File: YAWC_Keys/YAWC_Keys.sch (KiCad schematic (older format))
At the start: 19 parts, among them P1 K1, P10 K10, P11 K11, P2 K2, P3 K3, P4 K4, P5 K5, P6 K6, P7 K7, P8 K8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

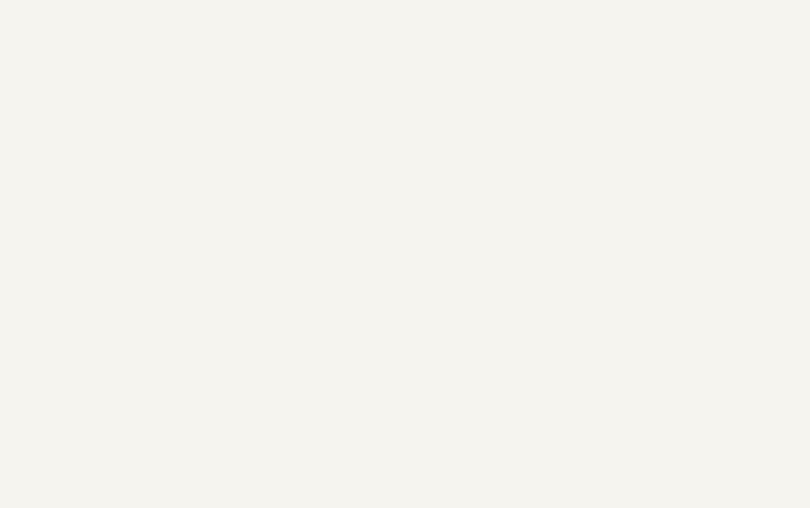
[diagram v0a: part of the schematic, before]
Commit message: Add route plugs for breath amp through to main board via keys. Add straight 1x6 header
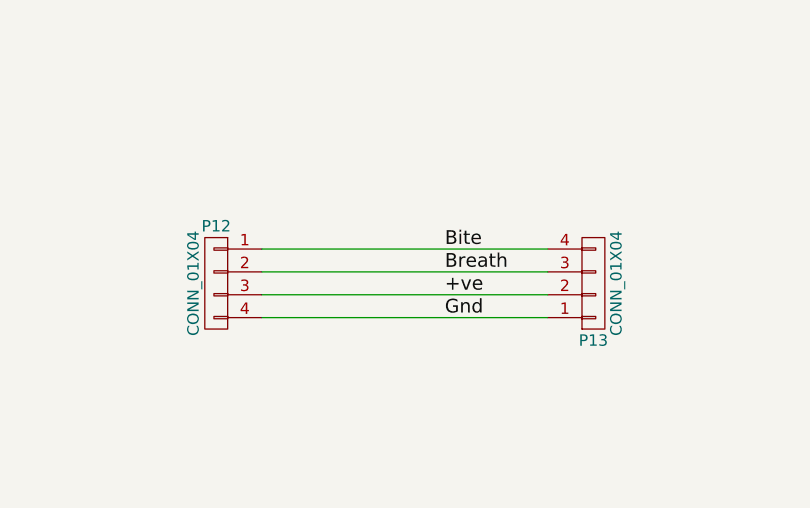
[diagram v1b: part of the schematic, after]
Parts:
- added P12: CONN_01X04, My_Pin_Headers:Pin_Header_Angled_1x04, symbol CONN_01X04
- added P13: CONN_01X04, My_Pin_Headers:Pin_Header_Straight_1x04, symbol CONN_01X04
- PLh1: footprint PIN_Hdr:Pin_Header_1x05 -> My_Pin_Headers:Pin_Header_Straight_1x05
- PRh1: footprint PIN_Hdr:Pin_Header_1x06 -> My_Pin_Headers:Pin_Header_Straight_1x06
- PTh1: footprint PIN_Hdr:Pin_Header_Angled_1x05 -> My_Pin_Headers:Pin_Header_Angled_1x05
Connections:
- new net +ve: P12.3 (P3), P13.2 (P2)
- new net Bite: P12.1 (P1), P13.4 (P4)
- new net Breath: P12.2 (P2), P13.3 (P3)
- new net Gnd: P12.4 (P4), P13.1 (P1)
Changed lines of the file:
@@
 F 0 "PLh1" H 5750 2100 50  0000 C CNN
 F 1 "CONN_01X05" V 5850 1800 50  0000 C CNN
-F 2 "PIN_Hdr:Pin_Header_1x05" H 5750 1800 50  0001 C CNN
+F 2 "My_Pin_Headers:Pin_Header_Straight_1x05" H 5750 1800 50  0001 C CNN
 F 3 "" H 5750 1800 50  0000 C CNN
 	1    5750 1800
@@
 F 0 "PTh1" H 5900 4300 50  0000 C CNN
 F 1 "CONN_01X05" V 6000 4000 50  0000 C CNN
-F 2 "PIN_Hdr:Pin_Header_Angled_1x05" H 5900 4000 50  0001 C CNN
+F 2 "My_Pin_Headers:Pin_Header_Angled_1x05" H 5900 4000 50  0001 C CNN
 F 3 "" H 5900 4000 50  0000 C CNN
 	1    5900 4000
@@
 F 0 "PRh1" H 9600 2250 50  0000 C CNN
 F 1 "CONN_01X06" V 9700 1900 50  0000 C CNN
-F 2 "PIN_Hdr:Pin_Header_1x06" H 9600 1900 50  0001 C CNN
+F 2 "My_Pin_Headers:Pin_Header_Straight_1x06" H 9600 1900 50  0001 C CNN
 F 3 "" H 9600 1900 50  0000 C CNN
 	1    9600 1900
@@
 Text Notes 6850 1400 0    197  ~ 0
 Right Hand
+$Comp
+L CONN_01X04 P12
+U 1 1 56EFDACE
+P 7050 3950
+F 0 "P12" H 7050 4200 50  0000 C CNN
+F 1 "CONN_01X04" V 7150 3950 50  0000 C CNN
+F 2 "My_Pin_Headers:Pin_Header_Angled_1x04" H 7050 3950 50  0001 C CNN
+F 3 "" H 7050 3950 50  0000 C CNN
+	1    7050 3950
+	-1   0    0    -1
+$EndComp
+$Comp
+L CONN_01X04 P13
+U 1 1 56EFDC09
+P 8700 3950
+F 0 "P13" H 8700 4200 50  0000 C CNN
+F 1 "CONN_01X04" V 8800 3950 50  0000 C CNN
+F 2 "My_Pin_Headers:Pin_Header_Straight_1x04" H 8700 3950 50  0001 C CNN
+F 3 "" H 8700 3950 50  0000 C CNN
+	1    8700 3950
+	1    0    0    1
+$EndComp
+Wire Wire Line
+	7250 3800 8500 3800
+Wire Wire Line
+	7250 3900 8500 3900
+Wire Wire Line
+	7250 4000 8500 4000
+Wire Wire Line
+	7250 4100 8500 4100
+Text Label 8050 3800 0    60   ~ 0
+Bite
+Text Label 8050 3900 0    60   ~ 0
+Breath
+Text Label 8050 4000 0    60   ~ 0
++ve
+Text Label 8050 4100 0    60   ~ 0
+Gnd
 $EndSCHEMATC
